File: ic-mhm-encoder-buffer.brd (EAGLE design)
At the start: 68 x 58.3 mm, 35 parts, among them IC1 LS7183-SOIC, J1 2023960907, J2 2023960607, M1 BSS670S2LH6327XTSA1, SW1 CS-4-13NTA, U1 24LC16BT-I/MC, U2 D5V0F4U6S-7, U3 D5V0F4U6S-7, U4 D5V0F4U6S-7

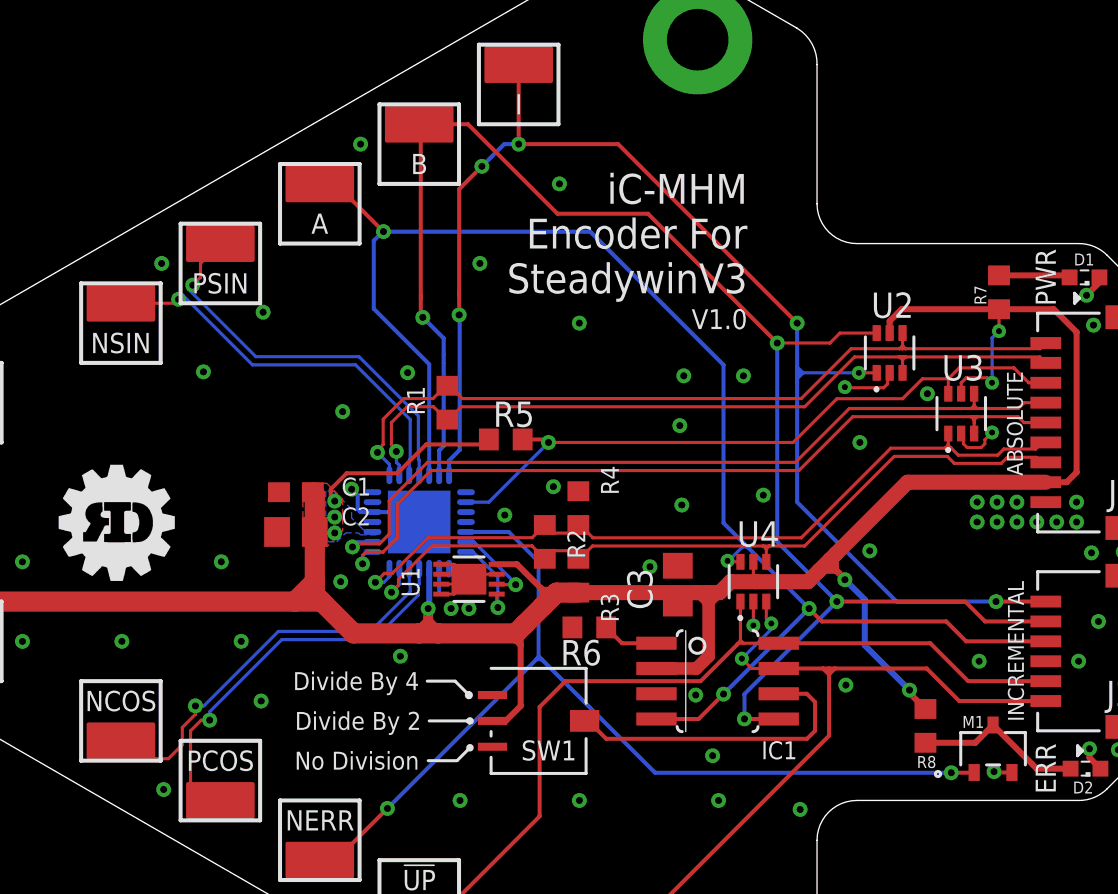
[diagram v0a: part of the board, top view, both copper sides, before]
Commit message: added verisons with buffers on ABI
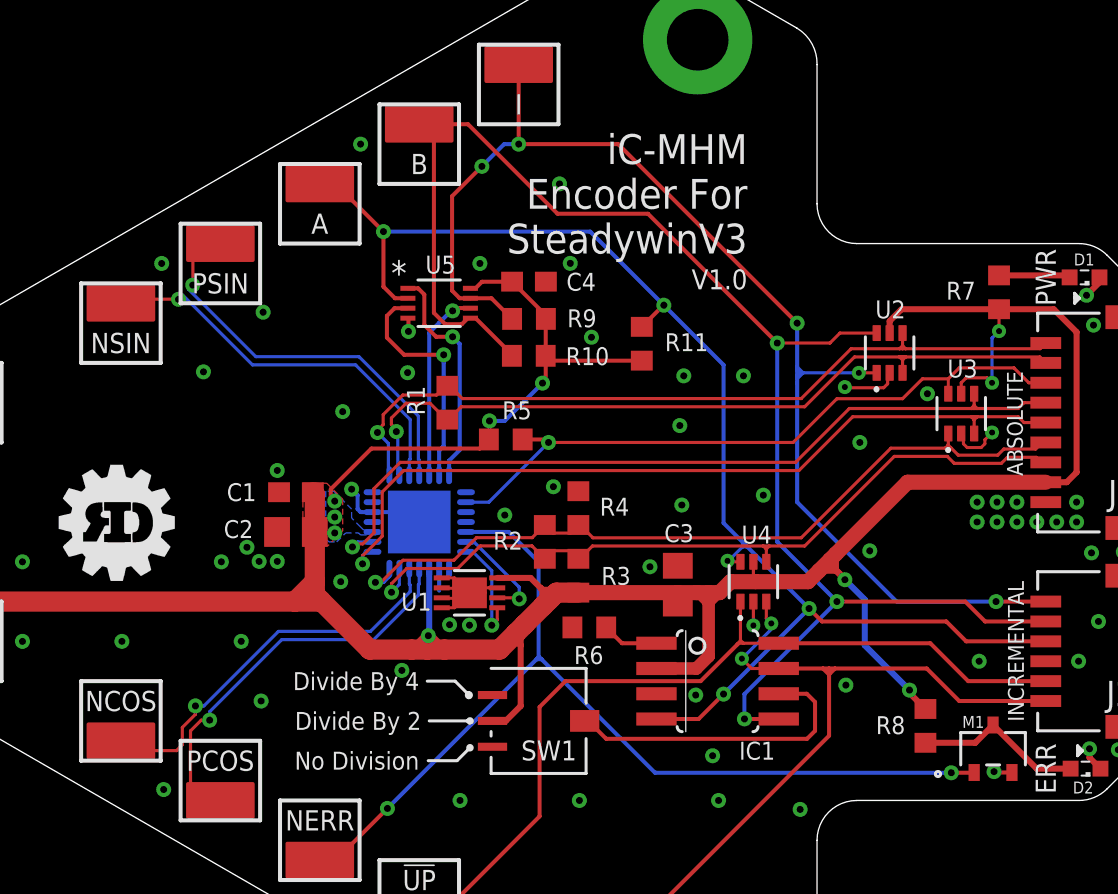
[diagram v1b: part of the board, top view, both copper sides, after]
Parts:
- added C4: 0.1uF, rcl:C0603
- added R10, R11, R9: 10K, rcl:R0603
- added U5: SN74LVC3G07QDCURQ1, ic-mhm:DCU8_TEX
- moved U1 0.69 mm to (2.53, -3.56)
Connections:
- new net ENC_A_MHM: U$1.P1, U5.6
- new net ENC_B_MHM: U$1.P2, U5.3
- new net ENC_Z_MHM: U$1.P3, U5.1
- net ENC_A: now also R11.2, U5.2; no longer U$1.P1
- net ENC_B: now also R10.2, U5.5; no longer U$1.P2
- net ENC_Z: now also R9.2, U5.7; no longer U$1.P3
- net GND: now also C4.2, U5.4
- net VDD: now also C4.1, R10.1, R11.1, R9.1, U5.8
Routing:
- net VDD: track 142.3 -> 161.6 mm, vias 8 -> 10
- net ENC_B_MHM: track 0.00 -> 11.7 mm, vias 0 -> 1
- net ENC_Z_MHM: track 0.00 -> 11.5 mm, vias 0 -> 1
- net ENC_A_MHM: track 0.00 -> 9.76 mm, vias 0 -> 1
- net ENC_A: track 76.7 -> 68.8 mm, vias 4 -> 5
- net ENC_Z: track 69.2 -> 63.4 mm, vias 6 -> 5
- net ENC_B: track 80.7 -> 77.4 mm, vias 4 -> 3
- net GND: track 23.6 -> 25.7 mm, vias 70 -> 76
- net SDA: track 4.37 -> 5.42 mm
- net SCL: track 4.38 -> 5.33 mm
- added copper zone on layer 15, net NC_1
- added copper zone on layer 2, net NC_1
